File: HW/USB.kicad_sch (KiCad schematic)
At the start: 27 parts, among them J3 USB4105-GF-A, Q1 PMV30XPEAR, Q2 BC857BS, U5 USBLC6-2P6, U6 CH340X

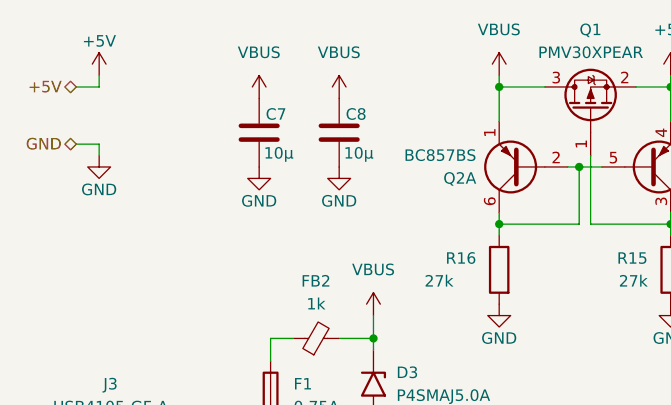
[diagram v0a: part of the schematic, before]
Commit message: Added uart and i2c to jtag connector, docs added
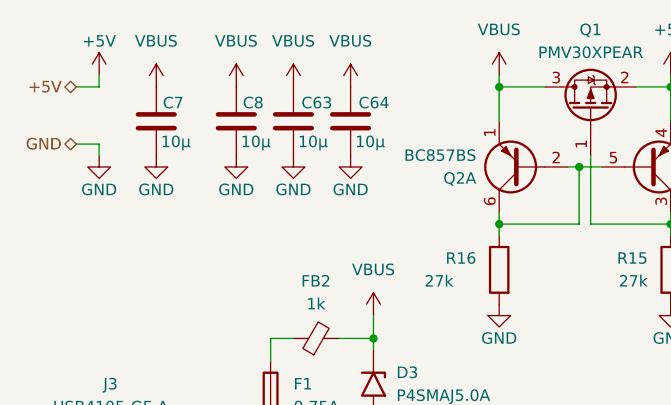
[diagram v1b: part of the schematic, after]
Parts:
- added C63, C64: 10µ, Capacitor_SMD:C_0402_1005Metric, symbol Device:C
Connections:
- net GND: now also C63.2, C64.2
- net VBUS: now also C63.1, C64.1
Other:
- moved on the sheet: C7, C8

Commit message: cleaned up and added missing files
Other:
- moved on the sheet: C7
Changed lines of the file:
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@@
 	(symbol
 		(lib_id "power:GND")
-		(at 34.29 31.75 0)
+		(at 36.83 31.75 0)
 		(unit 1)
 		(exclude_from_sim no)
@@
 		(dnp no)
 		(property "Reference" "#PWR028"
-			(at 34.29 38.1 0)
+			(at 36.83 38.1 0)
 			(effects
 				(font
@@
 		)
 		(property "Value" "GND"
-			(at 34.29 35.56 0)
+			(at 36.83 35.56 0)
 			(effects
 				(font
@@
 		)
 		(property "Footprint" ""
-			(at 34.29 31.75 0)
+			(at 36.83 31.75 0)
 			(effects
 				(font
@@
 		)
 		(property "Datasheet" ""
-			(at 34.29 31.75 0)
+			(at 36.83 31.75 0)
 			(effects
 				(font
@@
 		)
 		(property "Description" "Power symbol creates a global label with name \"GND\" , ground"
-			(at 34.29 31.75 0)
+			(at 36.83 31.75 0)
 			(effects
 				(font
@@
 	(symbol
 		(lib_id "Device:C")
-		(at 34.29 27.94 0)
+		(at 36.83 27.94 0)
 		(unit 1)
 		(exclude_from_sim no)
@@
 		(dnp no)
 		(property "Reference" "C7"
-			(at 37.338 25.908 0)
+			(at 39.878 25.908 0)
 			(effects
 				(font
@@
 		)
 		(property "Value" "10µ"
-			(at 34.798 30.226 0)
+			(at 37.338 30.226 0)
 			(effects
 				(font
@@
 		)
 		(property "Footprint" "Capacitor_SMD:C_0402_1005Metric"
-			(at 35.2552 31.75 0)
+			(at 37.7952 31.75 0)
 			(effects
 				(font
@@
 		)
 		(property "Datasheet" "~"
-			(at 34.29 27.94 0)
+			(at 36.83 27.94 0)
 			(effects
 				(font
@@
 		)
 		(property "Description" "Unpolarized capacitor"
-			(at 34.29 27.94 0)
+			(at 36.83 27.94 0)
 			(effects
 				(font
@@
 		)
 		(property "Model" "GRM155R60J106ME05D"
-			(at 34.29 27.94 0)
+			(at 36.83 27.94 0)
 			(effects
 				(font
@@
 		)
 		(property "Manufacturer" "Murata"
-			(at 34.29 27.94 0)
+			(at 36.83 27.94 0)
 			(effects
 				(font
@@
 		)
 		(property "JLCPCB" "C15525"
-			(at 34.29 27.94 0)
+			(at 36.83 27.94 0)
 			(effects
 				(font
@@
 	(symbol
 		(lib_id "power:VBUS")
-		(at 34.29 24.13 0)
+		(at 36.83 24.13 0)
 		(unit 1)
 		(exclude_from_sim no)
@@
 		(fields_autoplaced yes)
 		(property "Reference" "#PWR027"
-			(at 34.29 27.94 0)
+			(at 36.83 27.94 0)
 			(effects
 				(font
@@
 		)
 		(property "Value" "VBUS"
-			(at 34.29 19.05 0)
+			(at 36.83 19.05 0)
 			(effects
 				(font
@@
 		)
 		(property "Footprint" ""
-			(at 34.29 24.13 0)
+			(at 36.83 24.13 0)
 			(effects
 				(font
@@
 		)
 		(property "Datasheet" ""
-			(at 34.29 24.13 0)
+			(at 36.83 24.13 0)
 			(effects
 				(font
@@
 		)
 		(property "Description" "Power symbol creates a global label with name \"VBUS\""
-			(at 34.29 24.13 0)
-			(effects
-				(font
+			(at 36.83 24.13 0)
+			(effects
+				(font
